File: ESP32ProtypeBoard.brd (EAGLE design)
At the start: 78.7 x 80 mm, 108 parts, among them IC1 SOIC-8, IC2 SI4431BDY, IC4 LMC555*, Q1 MMBT3904*, Q2 MMBT3904, Q3 MMBT3904, U2 ESP-WROOM-32

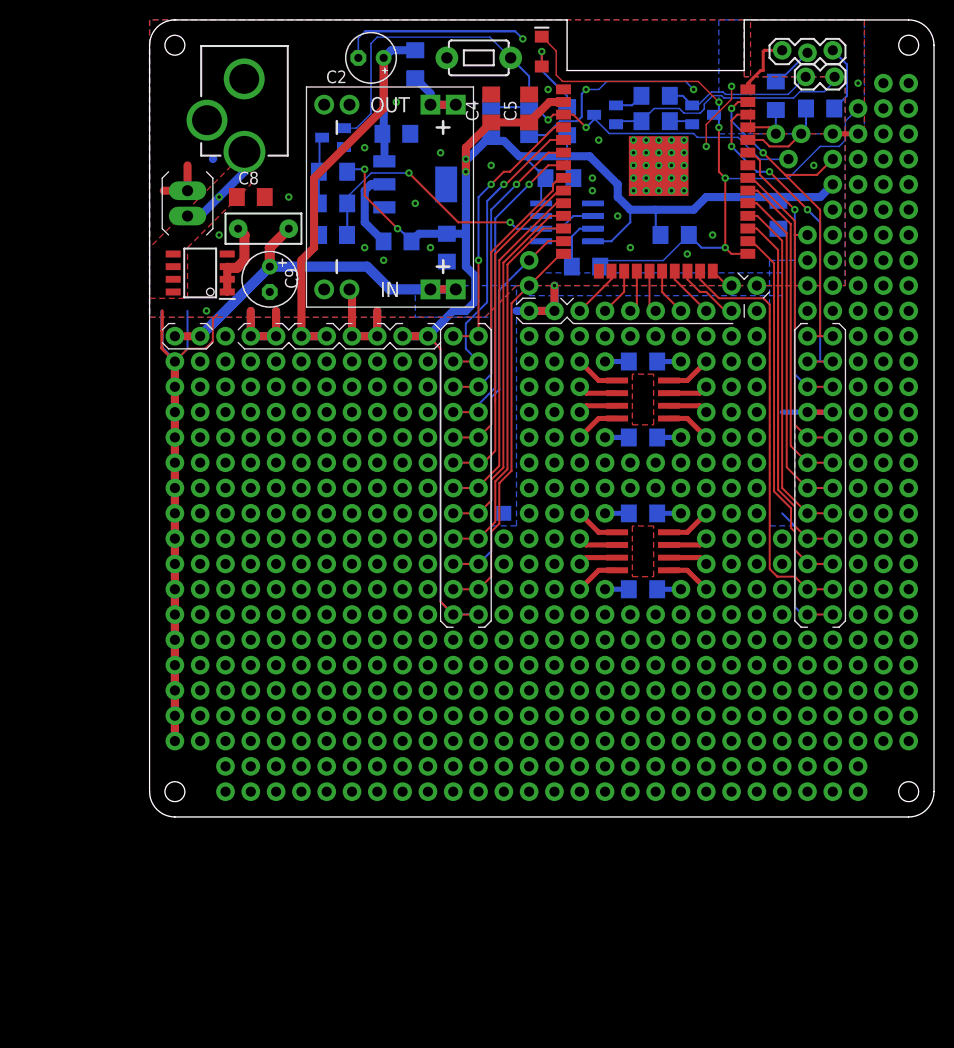
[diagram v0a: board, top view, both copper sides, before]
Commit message: Completely new layout of the board
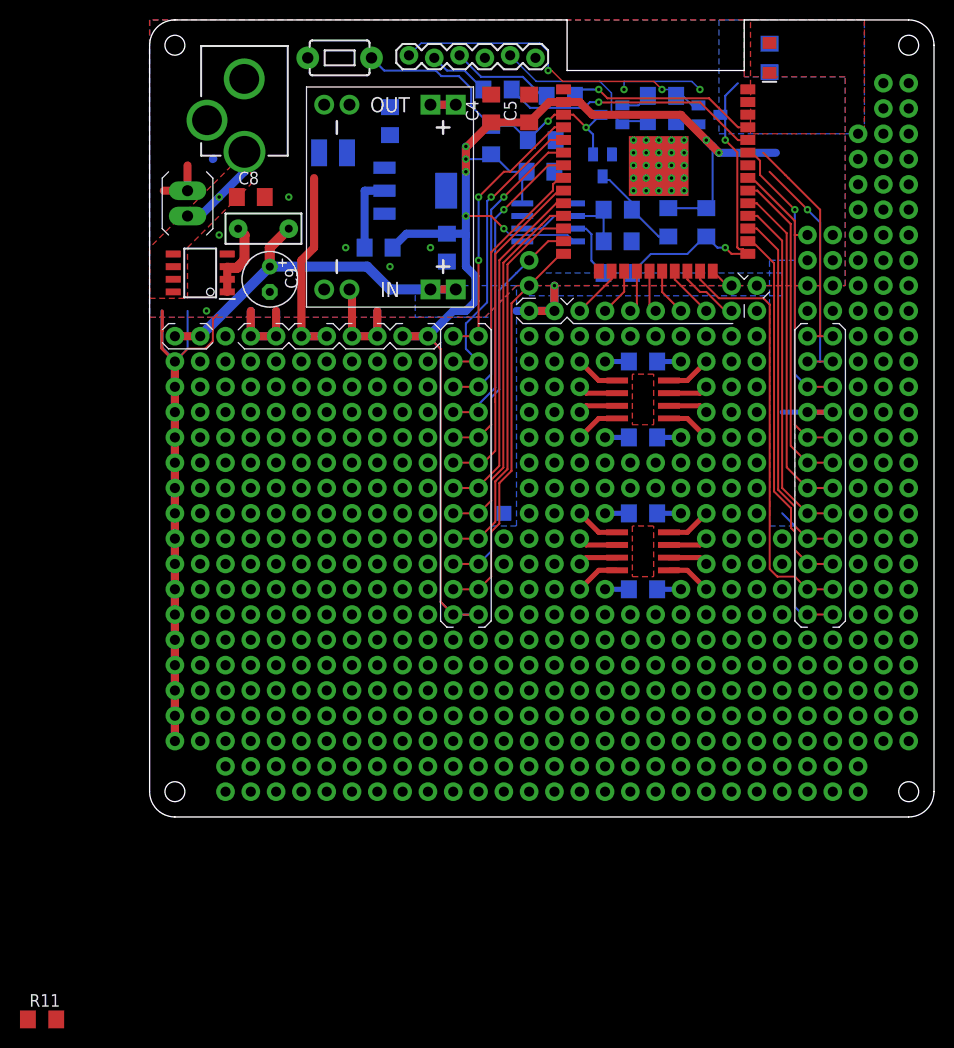
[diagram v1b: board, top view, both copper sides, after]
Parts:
- removed C11: (no value), rcl:C1206
- removed C7: 4.7uF, rcl:C1206
- removed CTRL: (no value), SparkFun-Connectors:1X02_LOCK
- removed J54, J_EN: (no value), SparkFun-Connectors:1X01_NO_SILK
- removed J56: (no value), SparkFun-Connectors:1X04_NO_SILK
- removed UART1: (no value), SparkFun-Connectors:1X02_NO_SILK
- added R11: 10K, eagle-ltspice:R1206
- C2: device rcl:E2,5-5 -> rcl:C1210
- UART: device SparkFun-Connectors:1X03_LOCK -> SparkFun-Connectors:1X06_LOCK
- moved R4 34.0 mm to (52.1, 59.7), turned to 270 degrees
- moved R8 32.4 mm to (34.9, 73.0), turned to 180 degrees
- moved C1 28.6 mm to (47.0, 57.8), turned to 0 degrees
- moved R6 28.6 mm to (47.0, 61.0), turned to 0 degrees
- moved Q1 27.2 mm to (45.5, 65.4), turned to 180 degrees
- moved UART 24.8 mm to (38.7, 76.2), turned to 180 degrees
- moved D2 22.9 mm to (62.2, 76.2), turned to 270 degrees
- moved R7 21.6 mm to (41.3, 72.4), turned to 180 degrees
- moved R1 21.3 mm to (62.2, 76.2)
- moved RESET 14.0 mm to (19.1, 76.2)
- moved C2 10.3 mm to (18.4, 66.7), flipped to the bottom, turned to 0 degrees
- moved PPTC2 6.25 mm to (24.1, 69.8), turned to 270 degrees
- moved R2 3.42 mm to (55.9, 59.7), turned to 270 degrees
- moved R9 3.24 mm to (47.0, 54.6)
- moved C6 2.29 mm to (39.4, 67.9), turned to 0 degrees
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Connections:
- new net USB+5V: UART.3
- new net VCC_EN: IC2.4, R11.1
- net +3V3: no longer C11.2, J56.2
- net +5V: now also C2.1; no longer C2.+, C7.1
- net DTR: now also UART.6; no longer CTRL.2
- net EN: no longer J_EN.1
- net GND: now also C2.2, R11.2; no longer C11.1, C2.-, C7.2, IC2.4, J56.4
- net IO0: no longer J54.1
- net IO23: no longer J56.3
- net RTS: now also UART.2; no longer CTRL.1
- net RXD0: no longer UART1.2
- net RXDU: now also UART.5; no longer UART.3
- net TXD0: no longer UART1.1
- net TXDU: now also UART.4; no longer UART.2
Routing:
- net GND: track 227.7 -> 180.8 mm, vias 52 -> 34
- net IO0: track 71.8 -> 34.0 mm, vias 4 -> 2
- net EN: track 64.9 -> 32.5 mm
- net +5V: track 50.6 -> 21.5 mm
- net TRIG: track 32.3 -> 12.1 mm, vias 2 -> 0
- net DTR: track 15.4 -> 33.3 mm, vias 0 -> 2
- net RXD0: track 8.89 -> 26.3 mm, vias 0 -> 1
- net TXD0: track 5.47 -> 19.2 mm, vias 0 -> 1
- net IO23: track 36.4 -> 23.3 mm, vias 2 -> 0
- net +3V3: track 180.4 -> 170.3 mm, vias 4 -> 7
- net IO22: track 35.6 -> 26.2 mm, vias 3 -> 1
- net D2A: track 8.12 -> 0.00 mm, vias 1 -> 0
- net RTS: track 25.1 -> 18.0 mm
- net TXDU: track 4.37 -> 10.4 mm
- net 5VOUT: track 8.38 -> 5.08 mm
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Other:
- board text added: "v1.1"
- board text removed: "0"
- board text removed: "EN"
- board text removed: "v1.0"

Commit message: Work in progress on 1.1
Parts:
- R11: value 10K -> 100K
- moved C2 0.64 mm to (18.4, 67.3)
- moved R7 0.64 mm to (41.3, 71.8)
- moved PPTC3 0.13 mm to (22.9, 57.1)
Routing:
- net +5V: track 21.5 -> 35.5 mm, vias 0 -> 2
- net +3V3: track 170.3 -> 157.4 mm, vias 7 -> 9
- net IO22: track 26.2 -> 33.4 mm
- net IO23: track 23.3 -> 29.6 mm
- net IO0: track 34.0 -> 38.6 mm, vias 2 -> 3
- net 5VOUT: track 5.08 -> 9.25 mm
- net D2A: track 0.00 -> 2.92 mm, vias 0 -> 1
- net GND: track 180.8 -> 183.5 mm, vias 34 -> 45
- net IO4: track 37.7 -> 38.3 mm
- net RXD0: track 26.3 -> 26.8 mm
- net DTR: track 33.3 -> 32.9 mm, vias 2 -> 0
- net VCC: vias 1 -> 2

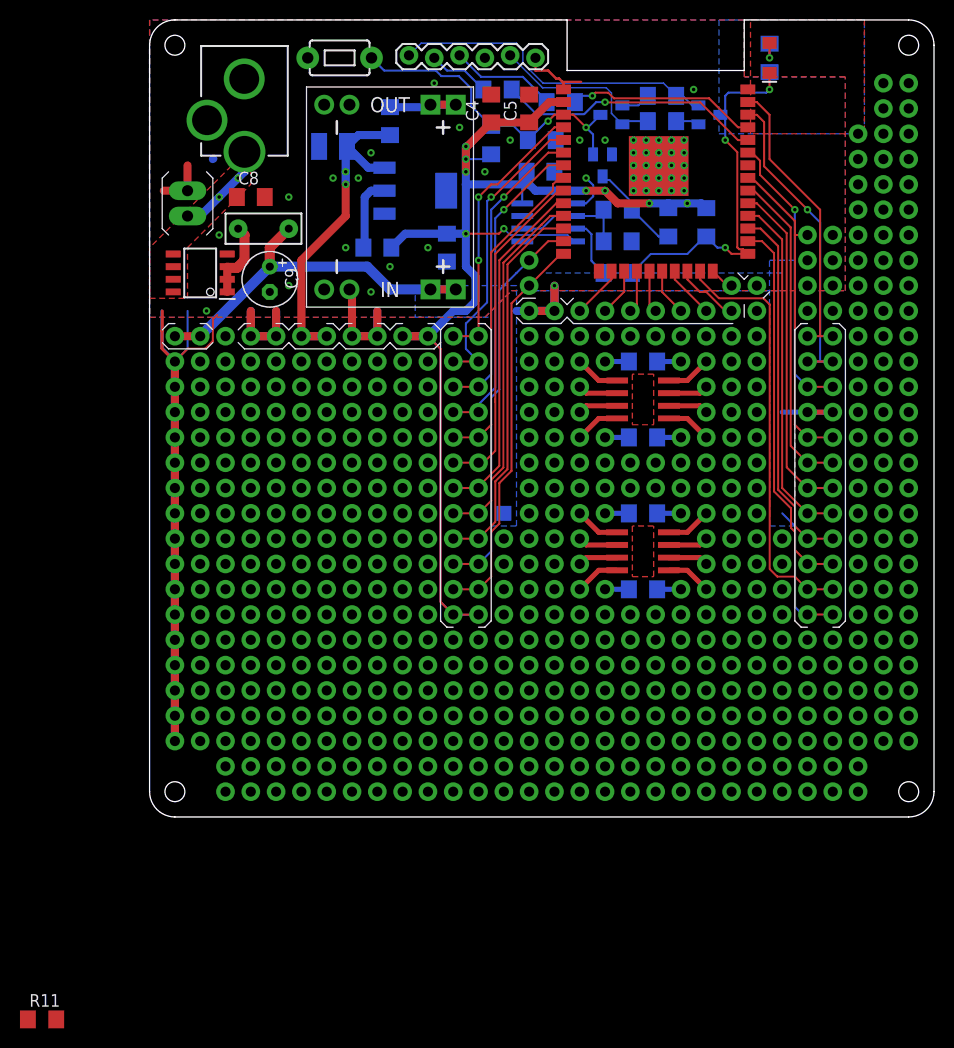
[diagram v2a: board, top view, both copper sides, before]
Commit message: Fixed uart pin order
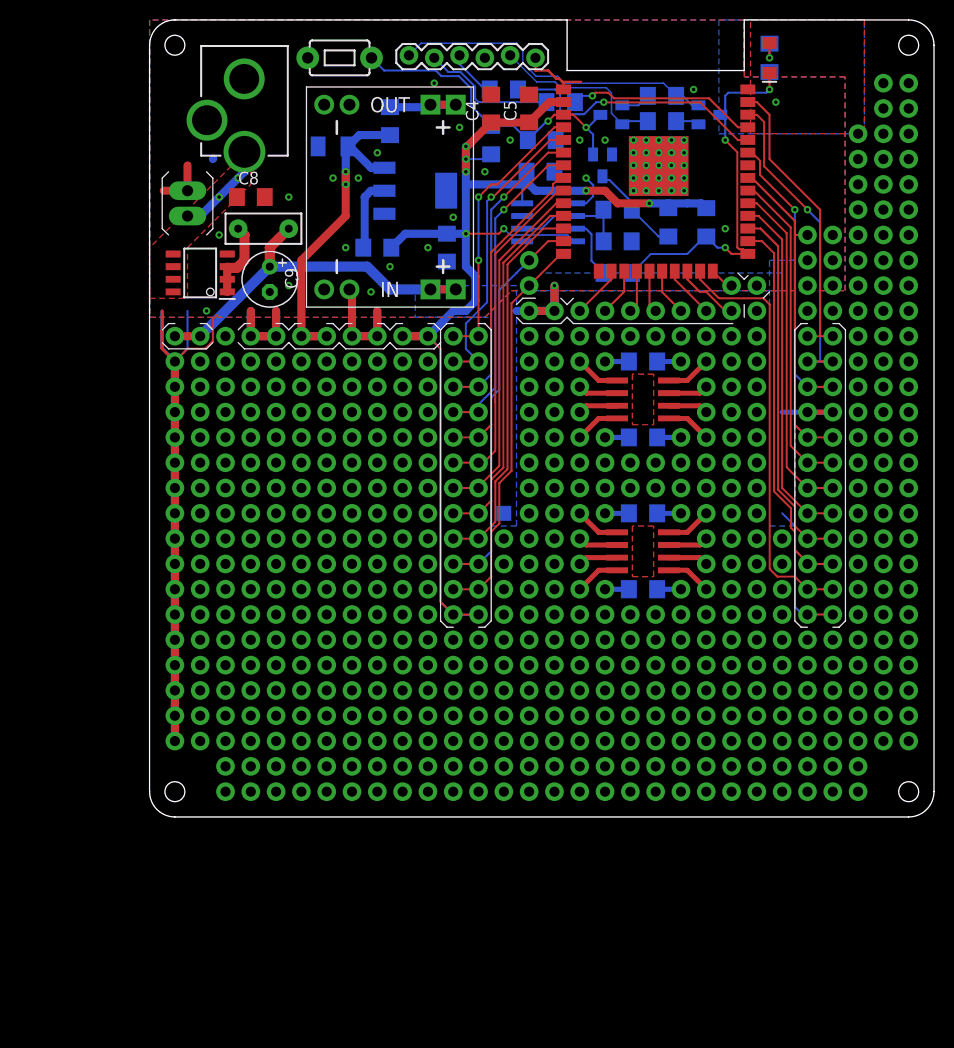
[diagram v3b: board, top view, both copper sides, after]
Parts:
- removed R11: 100K, eagle-ltspice:R1206
- C2: device rcl:C1210 -> rcl:C1206K
- moved R8 0.64 mm to (35.6, 73.0)
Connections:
- removed net VCC_EN: IC2.4, R11.1
- net GND: now also IC2.4; no longer R11.2
- net RXDU: now also UART.4; no longer UART.5
- net TXDU: now also UART.5; no longer UART.4
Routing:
- net TXDU: track 10.8 -> 13.8 mm
- net +5V: track 35.5 -> 37.0 mm
- net RXDU: track 6.24 -> 4.96 mm
- net IO0: track 38.6 -> 37.7 mm
- net GND: vias 45 -> 48
- net +3V3: vias 9 -> 7
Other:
- board text added: "NC"

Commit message: All connected
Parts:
- added J54: (no value), SparkFun-Connectors:1X10_NO_SILK
- C2: device rcl:C1206K -> rcl:C1210
- J8: device SparkFun-Connectors:1X04_NO_SILK -> SparkFun-Connectors:1X11_NO_SILK
- moved J17 9.16 mm to (66.0, 76.2)
- moved R1 6.35 mm to (62.2, 69.8)
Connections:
- net +3V3: now also J17.4, J17.5
- net GND: now also J17.2
- net IO22: now also J17.7
- net IO23: now also J17.3
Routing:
- net +3V3: track 157.4 -> 178.1 mm
- net GND: track 183.5 -> 201.9 mm, vias 48 -> 51
- net D2A: track 2.92 -> 8.09 mm
- net IO23: track 29.6 -> 32.2 mm
- net IO22: vias 1 -> 0

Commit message: Moving around some pins
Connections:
- net IO0: now also IO2.2
- net IO15: now also J16.1; no longer J12.11, J31.11
- net IO2: now also J12.11, J31.11; no longer IO2.2
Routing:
- net IO2: track 2.49 -> 41.1 mm
- net IO15: track 42.6 -> 7.84 mm
- net IO0: track 37.7 -> 41.4 mm, vias 3 -> 4
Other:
- board text added: "0"
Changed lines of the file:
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@@
 <layer number="50" name="dxf" color="7" fill="1" visible="no" active="no"/>
 <layer number="51" name="tDocu" color="7" fill="1" visible="yes" active="yes"/>
-<layer number="52" name="bDocu" color="7" fill="1" visible="no" active="yes"/>
+<layer number="52" name="bDocu" color="7" fill="1" visible="yes" active="yes"/>
 <layer number="53" name="tGND_GNDA" color="7" fill="9" visible="no" active="no"/>
 <layer number="54" name="bGND_GNDA" color="1" fill="9" visible="no" active="no"/>
@@
 <text x="55.88" y="51.943" size="0.8128" layer="51" font="vector" ratio="20" align="bottom-center">7</text>
 <text x="57.277" y="51.562" size="0.7112" layer="51" font="vector" ratio="20" align="bottom-center">8</text>
-<text x="57.023" y="52.959" size="0.8128" layer="51" font="vector" ratio="20" align="bottom-center">2</text>
+<text x="57.023" y="52.959" size="0.8128" layer="51" font="vector" ratio="20" align="bottom-center">0</text>
 <wire x1="59.69" y1="53.975" x2="59.055" y2="54.61" width="0.127" layer="21"/>
 <wire x1="61.595" y1="52.07" x2="62.23" y2="52.705" width="0.127" layer="21"/>
@@
 <text x="61.087" y="54.483" size="0.8128" layer="51" font="vector" ratio="20" align="bottom-center">GND</text>
 <text x="61.087" y="54.483" size="0.8128" layer="52" font="vector" ratio="20" rot="MR0" align="bottom-center">GND</text>
-<text x="58.42" y="54.483" size="0.8128" layer="52" font="vector" ratio="20" rot="MR0" align="bottom-center">2</text>
+<text x="58.42" y="54.483" size="0.8128" layer="52" font="vector" ratio="20" rot="MR0" align="bottom-center">0</text>
 <wire x1="1.27" y1="48.895" x2="1.905" y2="49.53" width="0.127" layer="22"/>
 <wire x1="1.905" y1="49.53" x2="2.54" y2="49.53" width="0.127" layer="22"/>
@@
 <wire x1="29.21" y1="48.895" x2="29.21" y2="47.625" width="0.127" layer="22"/>
 <wire x1="29.21" y1="48.895" x2="29.21" y2="47.625" width="0.127" layer="21"/>
-<wire x1="59.69" y1="50.165" x2="59.69" y2="51.435" width="0.127" layer="21"/>
-<wire x1="59.69" y1="51.435" x2="59.69" y2="50.165" width="0.127" layer="22"/>
 <text x="31.75" y="21.209" size="0.7112" layer="52" font="vector" ratio="20" rot="MR0" align="bottom-center">3V3</text>
 <text x="31.75" y="21.209" size="0.7112" layer="51" font="vector" ratio="20" align="bottom-center">3V3</text>
@@
 <text x="67.31" y="28.829" size="0.8128" layer="51" font="vector" ratio="20" align="bottom-center">16</text>
 <text x="67.31" y="26.289" size="0.8128" layer="51" font="vector" ratio="20" align="bottom-center">4</text>
-<text x="67.31" y="23.749" size="0.8128" layer="51" font="vector" ratio="20" align="bottom-center">15</text>
-<text x="67.31" y="23.749" size="0.8128" layer="52" font="vector" ratio="20" rot="MR0" align="bottom-center">15</text>
+<text x="67.31" y="23.749" size="0.8128" layer="51" font="vector" ratio="20" align="bottom-center">2</text>
+<text x="67.31" y="23.749" size="0.8128" layer="52" font="vector" ratio="20" rot="MR0" align="bottom-center">2</text>
 <text x="67.31" y="26.289" size="0.8128" layer="52" font="vector" ratio="20" rot="MR0" align="bottom-center">4</text>
 <text x="67.31" y="28.829" size="0.8128" layer="52" font="vector" ratio="20" rot="MR0" align="bottom-center">16</text>
@@
 <wire x1="46.609" y1="52.07" x2="47.371" y2="52.07" width="0.127" layer="52"/>
 <wire x1="44.069" y1="52.07" x2="44.831" y2="52.07" width="0.127" layer="52"/>
-<wire x1="59.69" y1="52.705" x2="59.69" y2="51.435" width="0.127" layer="51"/>
 <wire x1="60.325" y1="52.07" x2="59.69" y2="52.705" width="0.127" layer="51"/>
-<wire x1="59.69" y1="51.308" x2="59.69" y2="52.705" width="0.127" layer="52"/>
 <wire x1="59.69" y1="52.705" x2="60.325" y2="52.07" width="0.127" layer="52"/>
 <wire x1="62.23" y1="52.705" x2="62.23" y2="53.975" width="0.127" layer="52"/>
@@
 <wire x1="64.77" y1="65.405" x2="64.77" y2="66.04" width="0.127" layer="52"/>
 <text x="64.77" y="71.12" size="0.8128" layer="51" font="vector" ratio="20" align="center-right">22</text>
+<wire x1="59.69" y1="52.705" x2="59.055" y2="52.07" width="0.127" layer="51"/>
+<text x="62.23" y="50.8" size="0.7112" layer="51" font="vector" ratio="20" align="center-left">15</text>
+<text x="62.23" y="50.8" size="0.7112" layer="52" font="vector" ratio="20" rot="MR0" align="center-right">15</text>
 </plain>
 <attributes>
@@
 <contactref element="R2" pad="2"/>
 <wire x1="57.785" y1="57.15" x2="58.405" y2="56.53" width="0.2032" layer="1"/>
-<wire x1="58.405" y1="56.53" x2="60.05" y2="56.53" width="0.2032" layer="1"/>
+<wire x1="58.405" y1="56.53" x2="59.6364" y2="56.53" width="0.2032" layer="1"/>
 <contactref element="R9" pad="2"/>
 <contactref element="D2" pad="C"/>
@@
 <wire x1="55.88" y1="58.268" x2="56.998" y2="57.15" width="0.2032" layer="16"/>
 <wire x1="56.998" y1="57.15" x2="57.785" y2="57.15" width="0.2032" layer="16"/>
-<wire x1="60.05" y1="56.53" x2="59.5866" y2="56.9934" width="0.2032" layer="1"/>
-<wire x1="59.5866" y1="56.9934" x2="59.173" y2="56.9934" width="0.2032" layer="1"/>
-<wire x1="58.9934" y1="57.173" x2="59.173" y2="56.9934" width="0.2032" layer="1"/>
 <via x="57.785" y="67.945" extent="1-16" drill="0.35"/>
 <wire x1="57.785" y1="67.945" x2="58.9934" y2="66.7366" width="0.2032" layer="1"/>
@@
 <wire x1="62.23" y1="73.025" x2="62.23" y2="74.7" width="0.2032" layer="1"/>
 <wire x1="50.317" y1="56.515" x2="48.412" y2="54.61" width="0.2032" layer="16"/>
+<contactref element="IO2" pad="2"/>
+<wire x1="58.42" y1="53.34" x2="60.325" y2="55.245" width="0.2032" layer="16"/>
+<via x="60.325" y="55.245" extent="1-16" drill="0.35"/>
+<wire x1="60.325" y1="55.245" x2="60.325" y2="55.895" width="0.2032" layer="1"/>
+<wire x1="58.9934" y1="57.173" x2="59.6364" y2="56.53" width="0.2032" layer="1"/>
+<wire x1="59.6364" y1="56.53" x2="59.69" y2="56.53" width="0.2032" layer="1"/>
+<wire x1="59.69" y1="56.53" x2="60.05" y2="56.53" width="0.2032" layer="1"/>
+<wire x1="60.325" y1="55.895" x2="60.325" y2="56.255" width="0.2032" layer="1"/>
+<wire x1="60.325" y1="56.255" x2="60.05" y2="56.53" width="0.2032" layer="1"/>
 </signal>
 <signal name="IO34">
@@
 <signal name="IO15">
 <contactref element="U2" pad="23"/>
-<contactref element="J12" pad="11"/>
-<contactref element="J31" pad="11"/>
-<wire x1="66.04" y1="22.86" x2="68.58" y2="22.86" width="0.2032" layer="1"/>
+<contactref element="J16" pad="1"/>
+<wire x1="55.26" y1="54.79" x2="55.26" y2="53.96" width="0.2032" layer="1"/>
+<wire x1="59.69" y1="52.07" x2="60.96" y2="50.8" width="0.2032" layer="1"/>
 <wire x1="55.26" y1="53.96" x2="57.15" y2="52.07" width="0.2032" layer="1"/>
-<wire x1="55.26" y1="54.79" x2="55.26" y2="53.96" width="0.2032" layer="1"/>
-<wire x1="66.04" y1="22.86" x2="64.77" y2="24.13" width="0.2032" layer="1"/>
-<wire x1="64.77" y1="24.13" x2="63.00731875" y2="24.13" width="0.2032" layer="1"/>
-<wire x1="62.2536" y1="24.88371875" x2="63.00731875" y2="24.13" width="0.2032" layer="1"/>
-<wire x1="62.2536" y1="51.435" x2="62.2536" y2="24.88371875" width="0.2032" layer="1"/>
-<wire x1="57.15" y1="52.07" x2="61.6186" y2="52.07" width="0.2032" layer="1"/>
-<wire x1="61.6186" y1="52.07" x2="62.2536" y2="51.435" width="0.2032" layer="1"/>
+<wire x1="57.15" y1="52.07" x2="59.69" y2="52.07" width="0.2032" layer="1"/>
 </signal>
 <signal name="IO8">
@@
 <wire x1="53.99" y1="54.79" x2="53.99" y2="53.96" width="0.2032" layer="1"/>
 <wire x1="57.785" y1="50.8" x2="58.42" y2="50.8" width="0.2032" layer="1"/>
-<wire x1="57.785" y1="50.8" x2="55.88" y2="52.705" width="0.2032" layer="1"/>
-<wire x1="53.99" y1="53.96" x2="55.245" y2="52.705" width="0.2032" layer="1"/>
-<wire x1="55.245" y1="52.705" x2="55.88" y2="52.705" width="0.2032" layer="1"/>
+<wire x1="56.515" y1="52.07" x2="57.785" y2="50.8" width="0.2032" layer="1"/>
+<wire x1="55.88" y1="52.07" x2="56.515" y2="52.07" width="0.2032" layer="1"/>
+<wire x1="53.99" y1="53.96" x2="55.88" y2="52.07" width="0.2032" layer="1"/>
 </signal>
 <signal name="IO7">
@@
 <signal name="IO2">
 <contactref element="U2" pad="24"/>
-<contactref element="IO2" pad="2"/>
-<wire x1="57.98" y1="53.34" x2="56.53" y2="54.79" width="0.2032" layer="1"/>
-<wire x1="58.42" y1="53.34" x2="57.98" y2="53.34" width="0.2032" layer="1"/>
+<contactref element="J12" pad="11"/>
+<contactref element="J31" pad="11"/>
+<wire x1="66.04" y1="22.86" x2="68.58" y2="22.86" width="0.2032" layer="1"/>
+<wire x1="64.7464" y1="25.91628125" x2="63.99268125" y2="26.67" width="0.2032" layer="1"/>
+<wire x1="66.04" y1="22.86" x2="64.7464" y2="24.1536" width="0.2032" layer="1"/>
+<wire x1="64.7464" y1="25.91628125" x2="64.7464" y2="24.1536" width="0.2032" layer="1"/>
+<wire x1="62.2536" y1="51.4568" x2="62.2536" y2="27.42371875" width="0.2032" layer="1"/>
+<wire x1="62.2536" y1="27.42371875" x2="63.00731875" y2="26.67" width="0.2032" layer="1"/>
+<wire x1="63.00731875" y1="26.67" x2="63.99268125" y2="26.67" width="0.2032" layer="1"/>
+<wire x1="56.53" y1="54.79" x2="58.875" y2="54.79" width="0.2032" layer="1"/>
+<wire x1="58.875" y1="54.79" x2="59.69" y2="53.975" width="0.2032" layer="1"/>
+<wire x1="59.69" y1="53.975" x2="59.69" y2="52.705" width="0.2032" layer="1"/>
+<wire x1="59.69" y1="52.705" x2="60.325" y2="52.07" width="0.2032" layer="1"/>
+<wire x1="61.6404" y1="52.07" x2="62.2536" y2="51.4568" width="0.2032" layer="1"/>
+<wire x1="60.325" y1="52.07" x2="61.6404" y2="52.07" width="0.2032" layer="1"/>
 </signal>
 <signal name="N$13">
